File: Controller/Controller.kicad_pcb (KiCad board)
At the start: 2 copper layers, 151.1 x 80 mm, 66 parts, among them IC1 LMP7715MF, J1 Probes, J10 Chlorine Level, J11 EXT_2, J12 Temp2, J13 J1B1211CCD, J14 Acid Pump, J15 Chlorine Pump, J16 Filtration Pump, J17 Lighting, J18 Relay_Ext, J19 Flood sensor, J2 Display, J20 EXT_I2C, J21 EXT_UART, J22 1775485-2, J3 ESP32, J4 EXT_SPI, J5 EXT_1, J6 Pressure, J7 Acid Level, J8 VInput, J9 Temp1, K1 ALQ305, K2 ALQ305, K3 ALQ305, K4 ALQ305, K5 ALQ305, U1 Teensy4.1, U3 V7805-1000, U4 V7803-1000, U5 ULN2003A

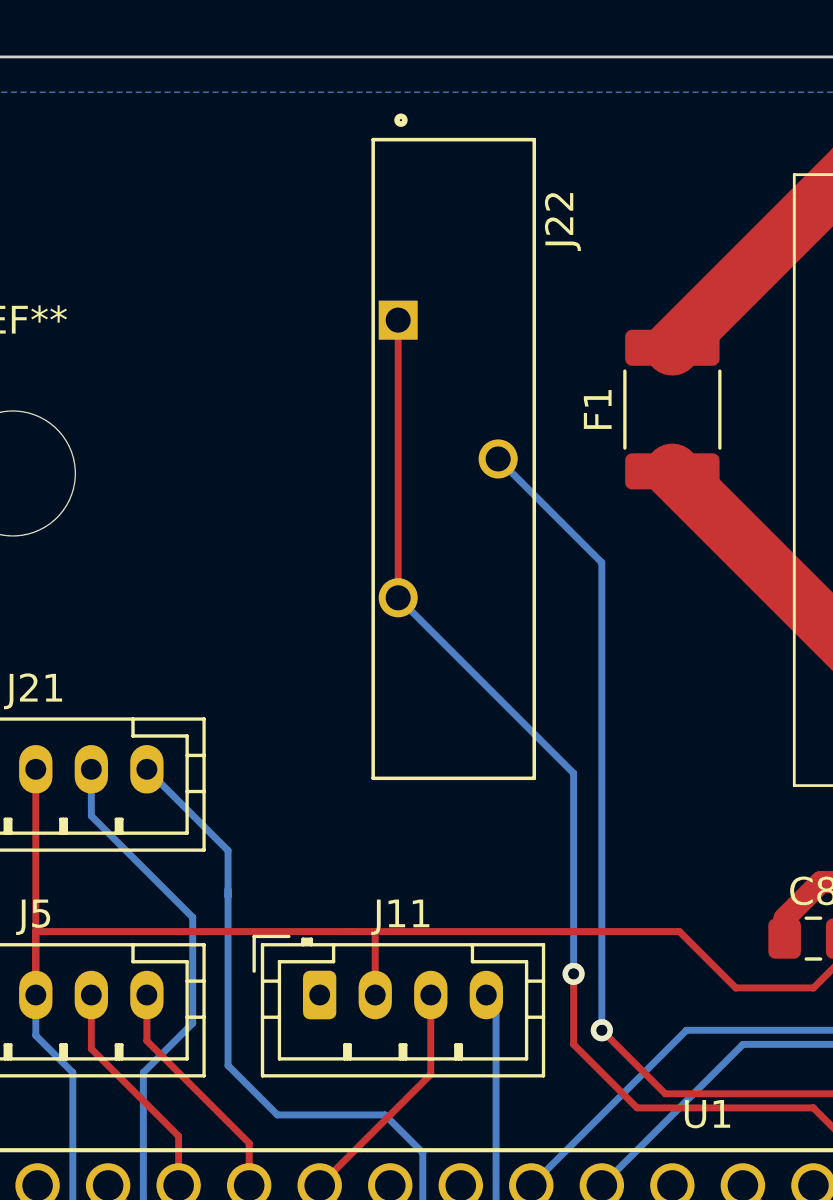
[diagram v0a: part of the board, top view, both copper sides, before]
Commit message: TE_1775485 -> keystone 1065
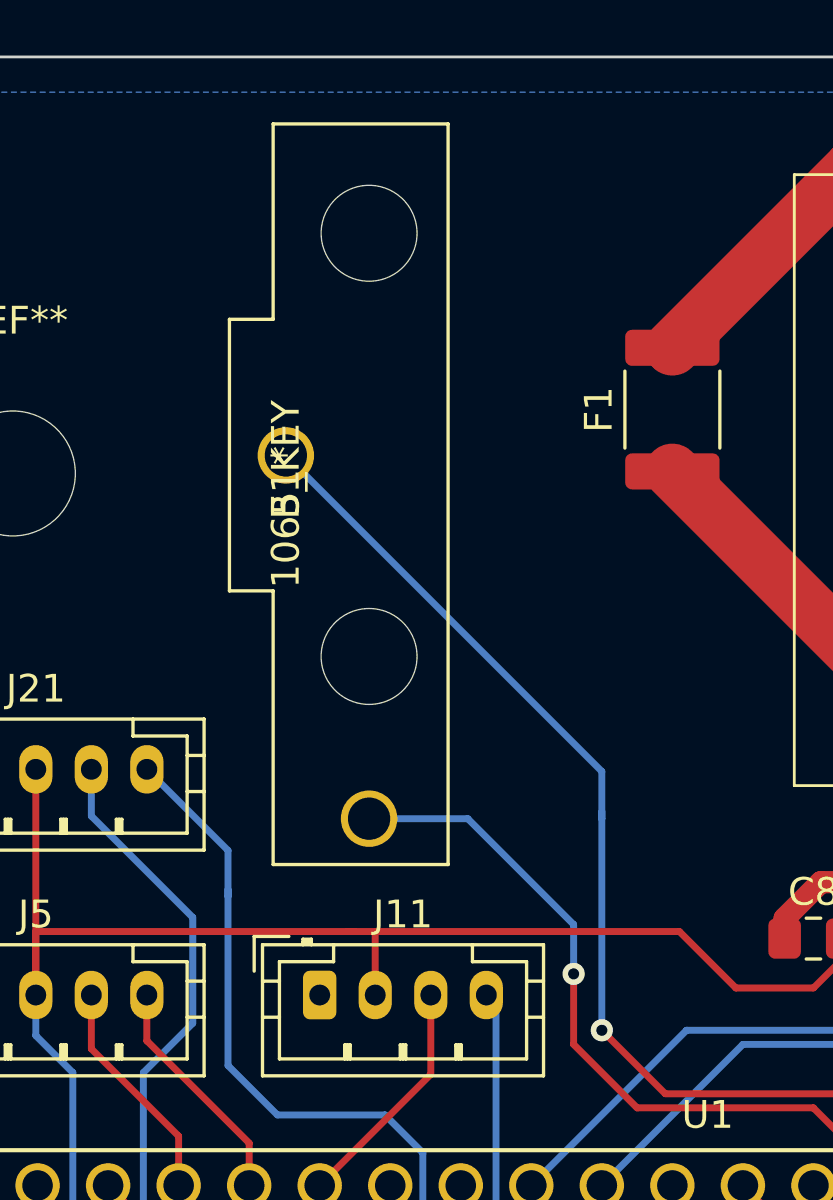
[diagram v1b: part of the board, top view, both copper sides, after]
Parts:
- removed J22: 1775485-2, snapeda:TE_1775485-2
- added B1: 1065_KEY, snapeda:1065, F.Cu at (44.5, 43.6)
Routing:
- net Net-(B1-Pad2): track 59.0 -> 43.6 mm
- net Net-(B1-Pad1): track 49.5 -> 53.1 mm

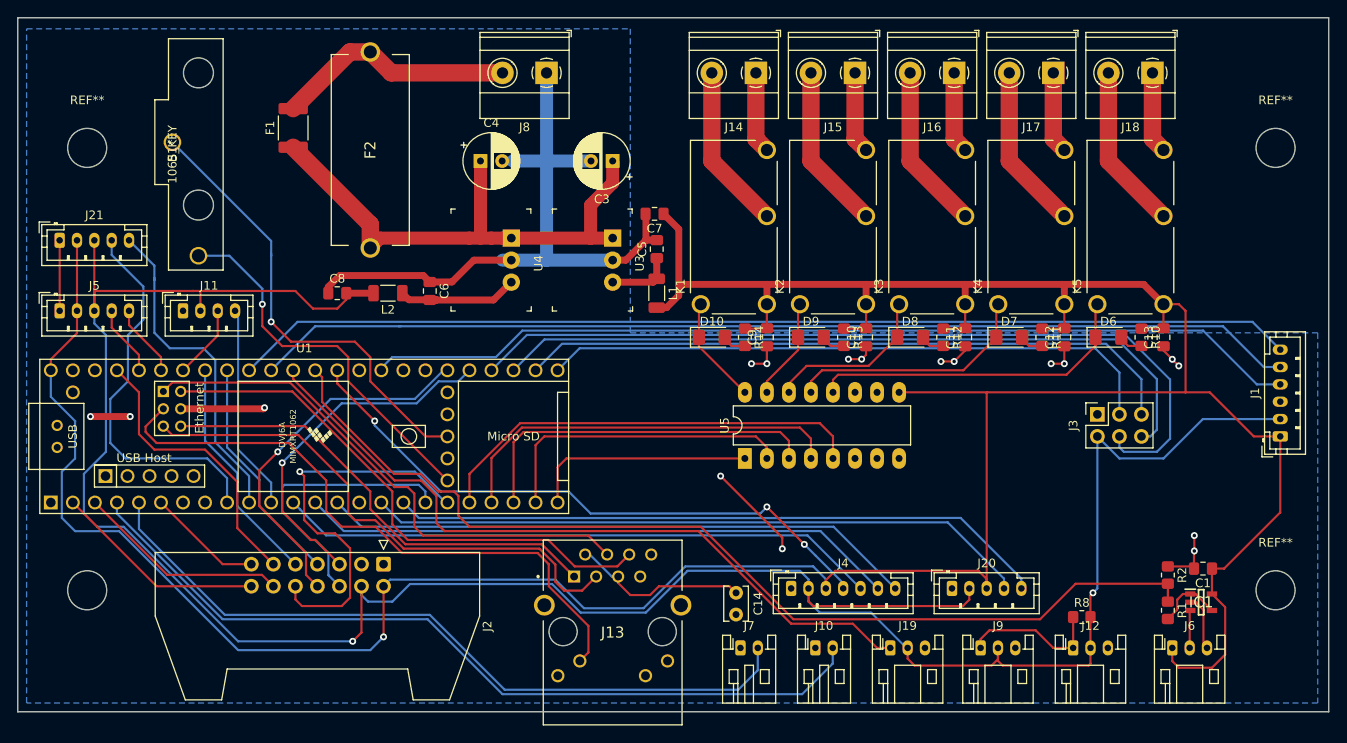
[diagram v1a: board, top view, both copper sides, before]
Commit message: make more room for relay
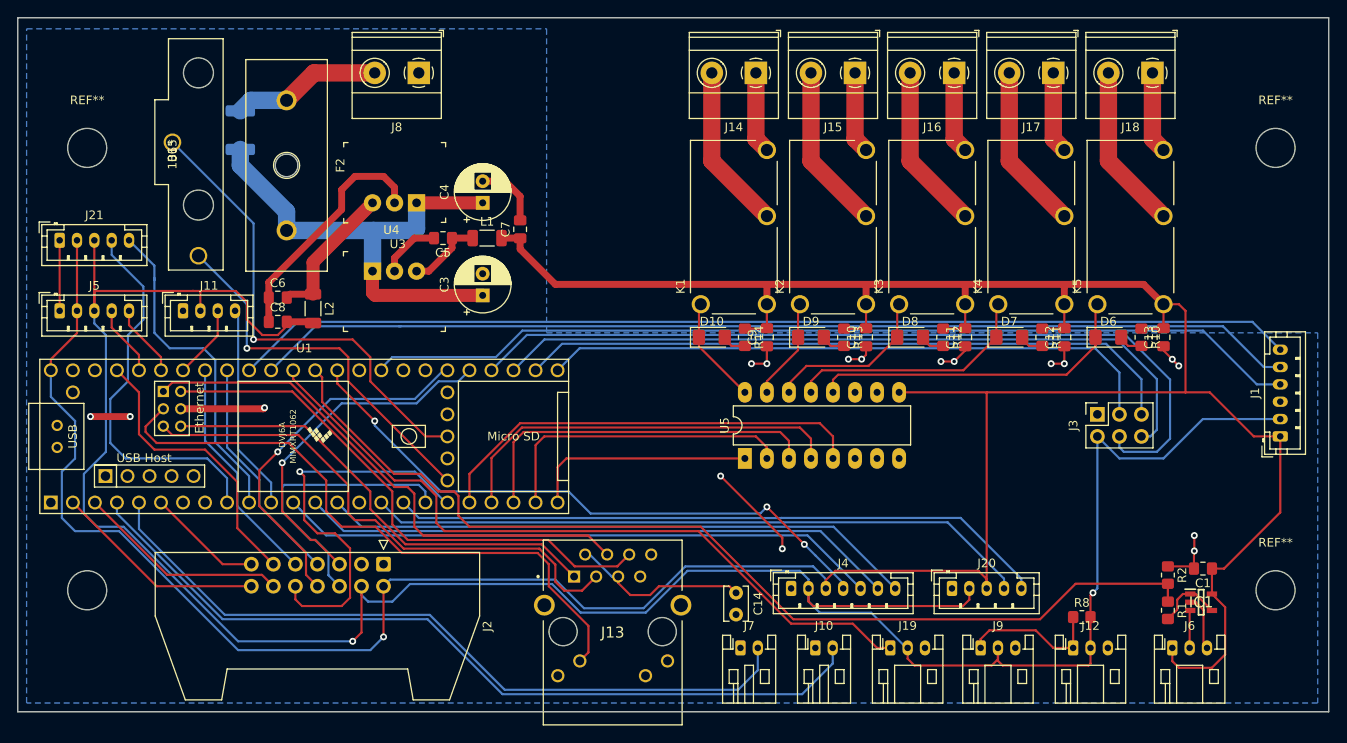
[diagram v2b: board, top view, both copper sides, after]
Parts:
- B1: value 1065_KEY -> 1065
- F1: moved to B.Cu
- F2: footprint SamacSys_Parts:696101000002 -> lib_divers:Fuse-PTF75_Stelvio
- moved U3 27.9 mm to (67.6, 58.4), turned to 0 degrees
- moved C5 24.7 mm to (75.7, 54.6), turned to 180 degrees
- moved C3 21.6 mm to (80.3, 61.2), turned to 90 degrees
- moved L1 20.6 mm to (80.8, 54.6), turned to 0 degrees
- moved C6 17.5 mm to (56.6, 61.5), turned to 0 degrees
- moved C7 15.6 mm to (84.6, 53.6), turned to 90 degrees
- moved J8 14.7 mm to (72.9, 35.6)
- moved U4 11.7 mm to (72.6, 50.5), turned to 180 degrees
- moved L2 8.82 mm to (60.7, 62.7), turned to 270 degrees
- moved C8 7.61 mm to (56.6, 64.3)
- moved F1 6.10 mm to (52.3, 42.2)
- moved F2 5.26 mm to (62.4, 46.2)
- moved C4 4.83 mm to (80.3, 50.5), turned to 90 degrees
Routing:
- net GND: track 140.5 -> 107.0 mm
- net Net-(F1-Pad2): track 27.8 -> 17.3 mm
- net +5V: track 388.0 -> 398.1 mm
- net Net-(C3-Pad1): track 62.5 -> 57.3 mm
- net +3V3: track 288.1 -> 283.4 mm
- net Net-(B1-Pad1): track 53.1 -> 55.2 mm
- net Net-(C6-Pad2): track 14.5 -> 16.6 mm
- net Net-(C5-Pad1): track 7.62 -> 8.71 mm

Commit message: ethernet diff tuning
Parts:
- removed C14: 0.1 uF, Capacitor_THT:C_Disc_D3.8mm_W2.6mm_P2.50mm
- added C2: 0.1uF, Capacitor_THT:CP_Radial_D5.0mm_P2.50mm, F.Cu at (103.1, 101.3)
- added J22: J1B1211CCD, Connector_RJ:RJ45_Cetus_J1B1211CCD_Horizontal, F.Cu at (85.9, 93.5)
- J13: value J1B1211CCD -> Eth; footprint SamacSys_Parts:J1B1211CCD -> Connector_PinHeader_2.00mm:PinHeader_2x03_P2.00mm_Vertical
- moved J13 10.8 mm to (105.2, 95.8), turned to 180 degrees
- moved J2 1.52 mm to (67.3, 92.2)
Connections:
- J13 pad 1: ETH_TX+ -> /TX+
- J13 pad 2: Net-(C14-Pad1) -> /TX-
- J13 pad 3: ETH_TX- -> Net-(C2-Pad2)
- J13 pad 4: ETH_RX+ -> Net-(J13-Pad4)
- J13 pad 5: Net-(C14-Pad1) -> /RX-
- J13 pad 6: ETH_RX- -> /RX+
- U1 pad 60: ETH_RX+ -> (no net)
- U1 pad 61: ETH_LED -> (no net)
- U1 pad 62: ETH_TX- -> (no net)
- U1 pad 63: ETH_TX+ -> (no net)
- U1 pad 64: GND -> (no net)
- U1 pad 65: ETH_RX- -> (no net)
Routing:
- net ETH_LED: track 71.9 -> 0.00 mm
- net ETH_RX-: track 62.9 -> 0.00 mm
- net ETH_RX+: track 62.0 -> 0.00 mm
- net ETH_TX-: track 61.5 -> 0.00 mm
- net ETH_TX+: track 53.7 -> 0.00 mm
- net Net-(C2-Pad2): track 0.00 -> 50.3 mm
- net Net-(C2-Pad1): track 0.00 -> 23.7 mm
- net /TX+: track 0.00 -> 22.2 mm
- net /TX-: track 0.00 -> 21.4 mm
- net Net-(J13-Pad4): track 0.00 -> 20.6 mm, vias 0 -> 1
- net Net-(C14-Pad1): track 20.5 -> 0.00 mm
- net /RX+: track 0.00 -> 14.6 mm
- net /RX-: track 0.00 -> 14.2 mm
- net GND: track 107.0 -> 113.2 mm, vias 17 -> 21
- net +3V3: track 283.4 -> 287.3 mm
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
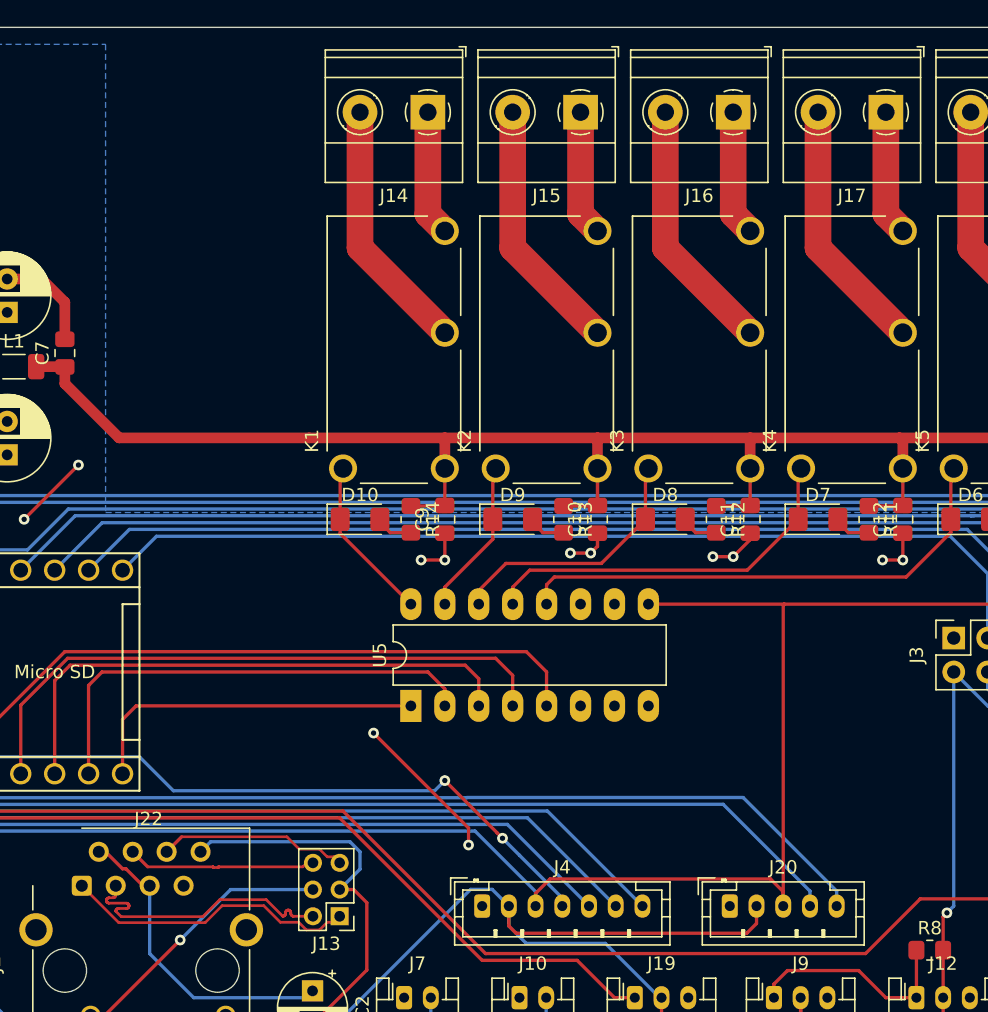
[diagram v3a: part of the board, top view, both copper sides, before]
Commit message: relay ethernet too small
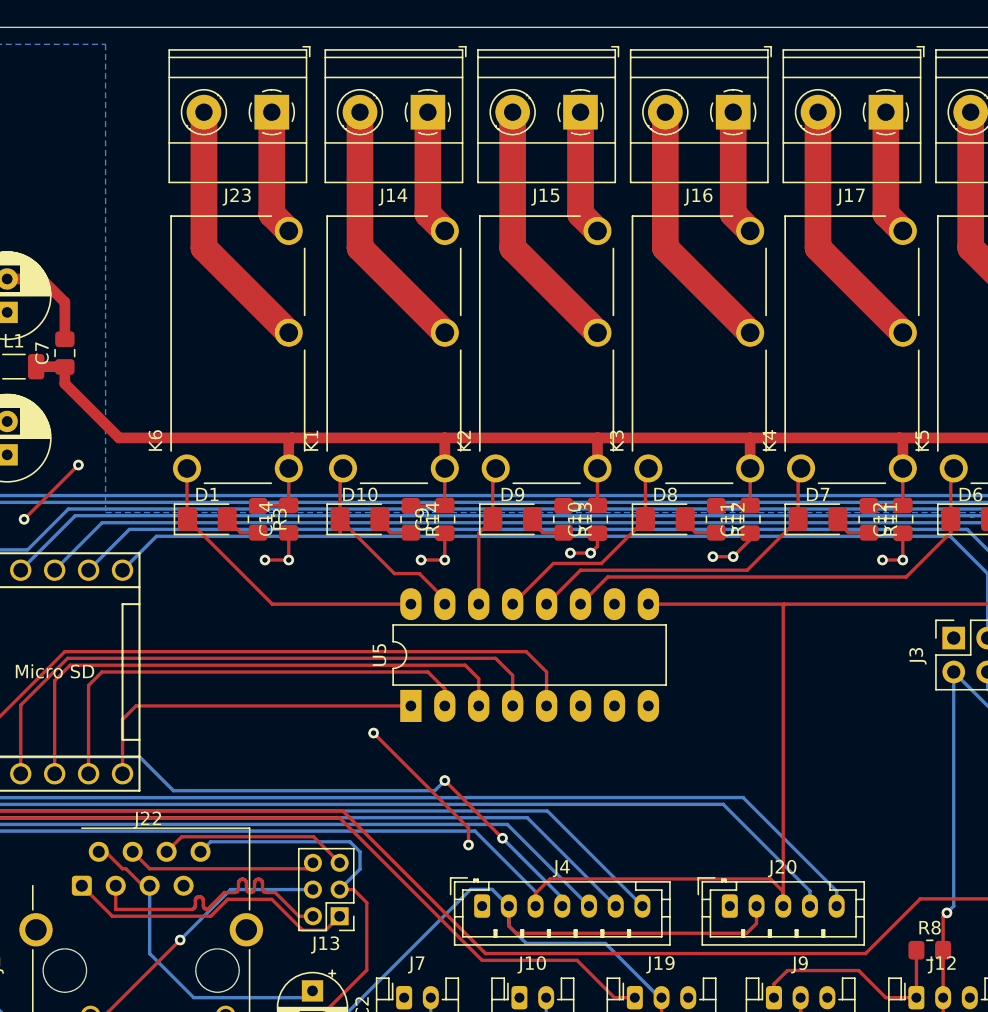
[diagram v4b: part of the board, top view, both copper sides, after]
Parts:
- added C14: 4.7uF, Capacitor_SMD:C_0805_2012Metric_Pad1.18x1.45mm_HandSolder, F.Cu at (101.3, 66.0)
- added D1: LED, LED_SMD:LED_1206_3216Metric_Pad1.42x1.75mm_HandSolder, F.Cu at (95.2, 66.0)
- added J23: Relay_Ext, TerminalBlock_Phoenix:TerminalBlock_Phoenix_MKDS-1,5-2-5.08_1x02_P5.08mm_Horizontal, F.Cu at (100.1, 35.6)
- added K6: ALQ305, snapeda:RELAY_ALQ305, F.Cu at (97.5, 53.3)
- added R3: 180, Resistor_SMD:R_0805_2012Metric_Pad1.20x1.40mm_HandSolder, F.Cu at (99.1, 66.0)
- J18: value Relay_Ext -> Air
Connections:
- U5 pad 11: (no net) -> Net-(D6-Pad1)
- U5 pad 12: Net-(D6-Pad1) -> Net-(D7-Pad1)
- U5 pad 13: Net-(D7-Pad1) -> Net-(D8-Pad1)
- U5 pad 14: Net-(D8-Pad1) -> Net-(D9-Pad1)
- U5 pad 15: Net-(D9-Pad1) -> Net-(D10-Pad1)
- U5 pad 16: Net-(D10-Pad1) -> Net-(D1-Pad1)
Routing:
- net Net-(D1-Pad1): track 0.00 -> 23.2 mm
- net Net-(J23-Pad2): track 0.00 -> 19.1 mm
- net Net-(J23-Pad1): track 0.00 -> 9.42 mm
- net +5V: track 398.0 -> 405.5 mm
- net GND: track 113.2 -> 117.0 mm, vias 21 -> 23
- net Net-(D10-Pad1): track 12.4 -> 15.9 mm
- net Net-(D6-Pad1): track 38.2 -> 34.8 mm
- net Net-(D7-Pad1): track 28.6 -> 25.4 mm
- net Net-(D8-Pad1): track 19.6 -> 16.5 mm
- net Net-(D1-Pad2): track 0.00 -> 2.74 mm
- net /TX-: track 21.4 -> 22.2 mm

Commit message: JST to SMT
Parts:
- J10, J7: footprint Connector_JST:JST_PH_S2B-PH-K_1x02_P2.00mm_Horizontal -> Connector_JST:JST_PH_S2B-PH-SM4-TB_1x02-1MP_P2.00mm_Horizontal
- J12, J19, J6, J9: footprint Connector_JST:JST_PH_S3B-PH-K_1x03_P2.00mm_Horizontal -> Connector_JST:JST_PH_S3B-PH-SM4-TB_1x03-1MP_P2.00mm_Horizontal
- moved C2 9.52 mm to (110.0, 94.7), turned to 90 degrees
- moved R2 5.64 mm to (158.5, 87.9)
- moved C1 5.64 mm to (162.5, 87.1)
- moved IC1 5.64 mm to (162.3, 91.0)
- moved R1 5.64 mm to (158.5, 91.9)
- moved J7 4.38 mm to (105.7, 102.6)
- moved J10 3.39 mm to (115.3, 102.6)
- moved R8 2.96 mm to (148.4, 95.5)
- moved J20 1.78 mm to (134.4, 93.2)
- moved J4 1.78 mm to (115.8, 93.2)
- moved J19 1.48 mm to (126.0, 102.6)
- moved J6 1.48 mm to (161.0, 102.6)
- moved J12 1.27 mm to (149.4, 102.6)
- moved J9 0.76 mm to (137.7, 102.6)
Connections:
- J12 pad 1: /Temp -> Temp
- J9 pad 1: /Temp -> Temp
- R8 pad 1: /Temp -> Temp
- U1 pad 20: Relay1 -> Relay5
- U1 pad 21: Relay2 -> Relay4
- U1 pad 23: Relay4 -> Relay2
- U1 pad 24: Relay5 -> Relay1
- U1 pad 31: (no net) -> Temp
- U1 pad 32: (no net) -> Relay6
- U5 pad 1: Relay5 -> Relay1
- U5 pad 2: Relay4 -> Relay2
- U5 pad 4: Relay2 -> Relay4
- U5 pad 5: Relay1 -> Relay5
- U5 pad 6: (no net) -> Relay6
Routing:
- net GND: track 117.0 -> 227.0 mm, vias 23 -> 27
- net Temp: track 0.00 -> 108.2 mm, vias 0 -> 2
- net Relay6: track 0.00 -> 57.1 mm
- net Relay5: track 26.1 -> 50.8 mm
- net Relay1: track 50.8 -> 26.1 mm
- net EXT_SCK: track 70.9 -> 92.5 mm
- net /Temp: track 16.5 -> 0.00 mm
- net Relay4: track 35.5 -> 46.2 mm
- net Relay2: track 46.2 -> 35.5 mm
- net Net-(C2-Pad2): track 50.3 -> 40.5 mm, vias 0 -> 1
- net +5V: track 405.5 -> 414.8 mm
- net Net-(C2-Pad1): track 23.7 -> 31.9 mm
- net +3V3: track 287.3 -> 279.6 mm, vias 2 -> 5
- net Pressure: track 117.0 -> 111.0 mm
- net Net-(IC1-Pad3): track 4.35 -> 7.94 mm
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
